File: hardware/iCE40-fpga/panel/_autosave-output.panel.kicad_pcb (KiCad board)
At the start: 4 copper layers, 45 x 48.4 mm, 138 parts, among them J1 USB_B_Micro, J2 JST_PH, J3 Feather, Q1 DMP2045U, U1 MCP73831-2-OT, U2 W25Q32JVZP, U3 AP2112K-3.3, U4 ICE40UP5K-SG48ITR, U5 NCV8114ASN120T1G, U6 93C46B, U7 FT2232H, X1 DSC6101CI1A

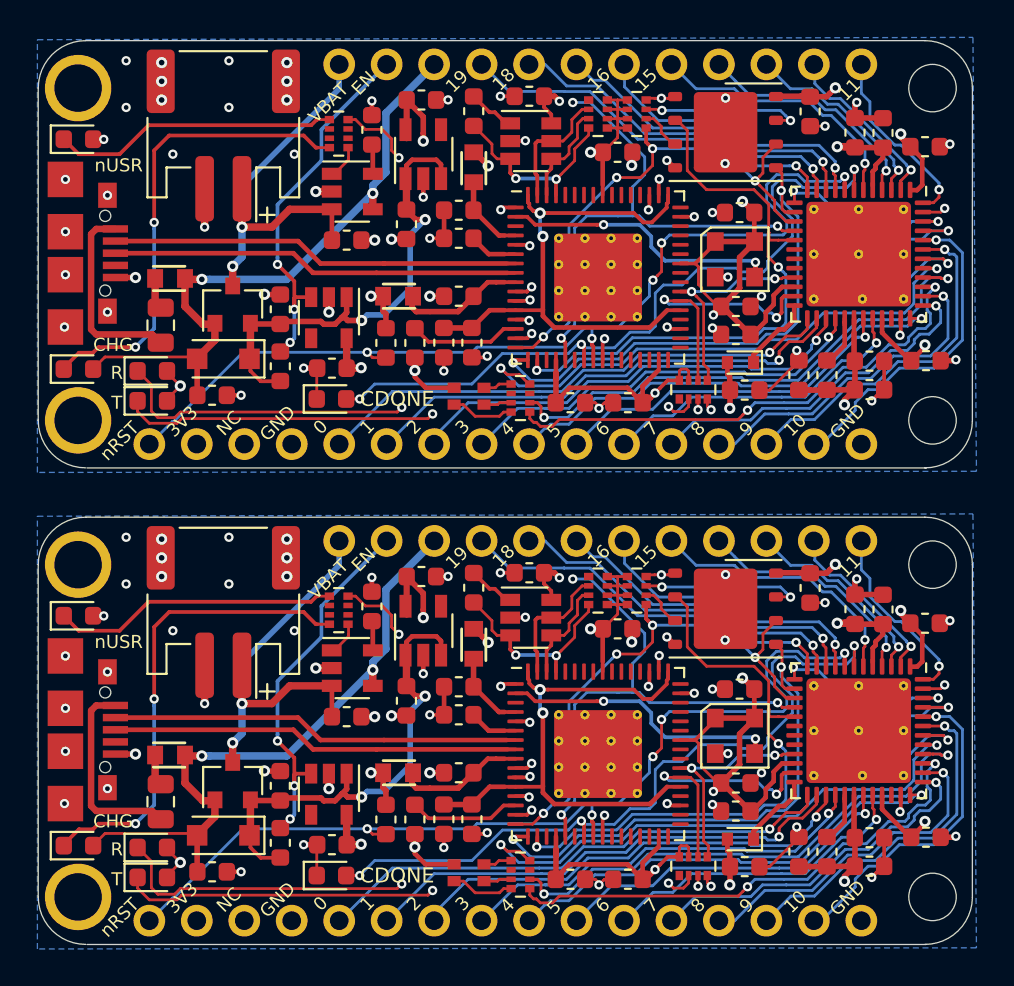
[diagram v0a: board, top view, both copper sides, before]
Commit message: moved battery connector and generated new gerbers for FPGA
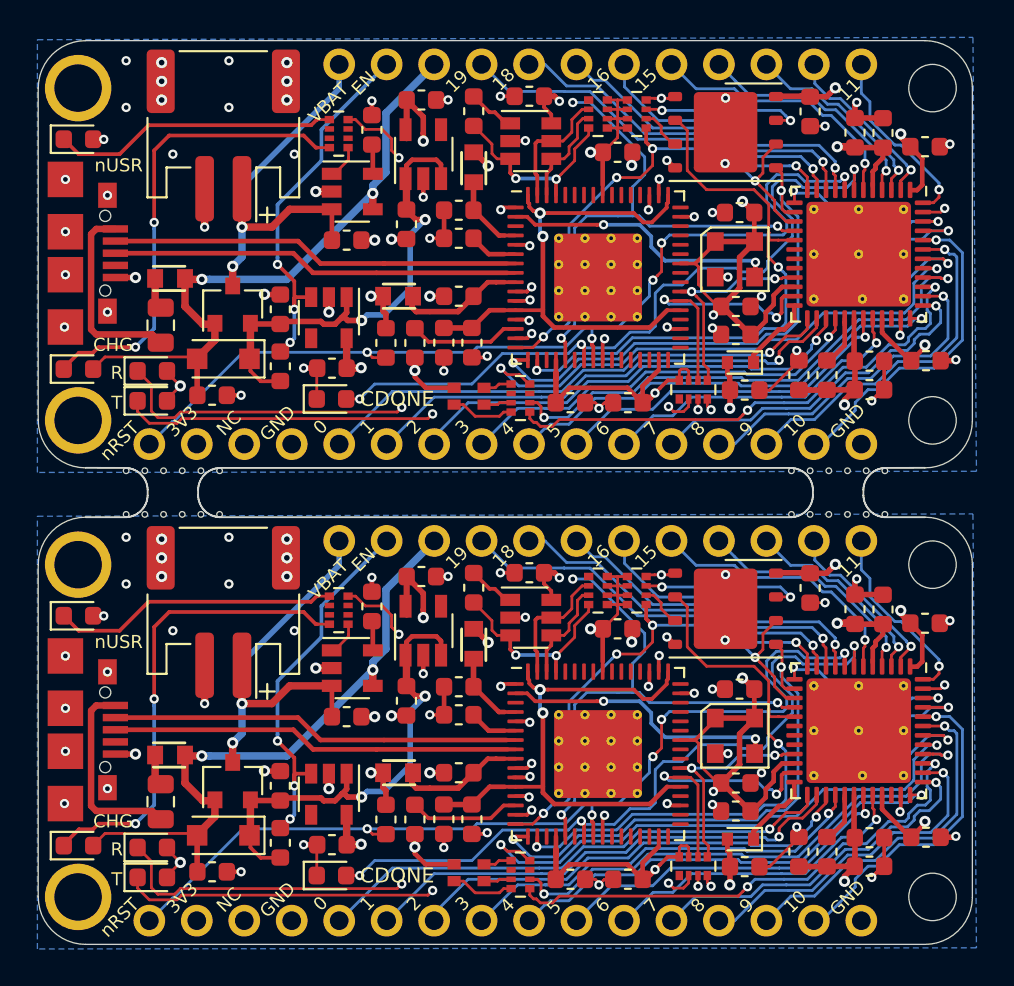
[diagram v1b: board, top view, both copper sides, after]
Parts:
- added ?: , holes, F.Cu at (72.1, 47.8)
- added ?: , holes, F.Cu at (67.1, 45.4)
- added ?: , holes, F.Cu at (31.5, 45.4)
- added ?: , holes, F.Cu at (36.5, 47.8)
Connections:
- net /FLASH_MISO|IO1 renamed /FLASH_MISOIO1
- net /FLASH_MOSI|IO0 renamed /FLASH_MOSIIO0
- net /FLASH_nHOLD|IO3 renamed /FLASH_nHOLDIO3
- net /FLASH_nWP|IO2 renamed /FLASH_nWPIO2
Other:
- board size 45 x 48.4 mm -> 44.9 x 48.4 mm
- board text added: "All"
- board text added: "JLCJLCJLC"
- board text added: "MLCC"
